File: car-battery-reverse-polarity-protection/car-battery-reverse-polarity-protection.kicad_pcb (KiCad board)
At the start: 2 copper layers, 64 x 75 mm, 10 parts, among them J1 Battery Connector, J2 Output, K1 AZ2150-1AE-24DEF

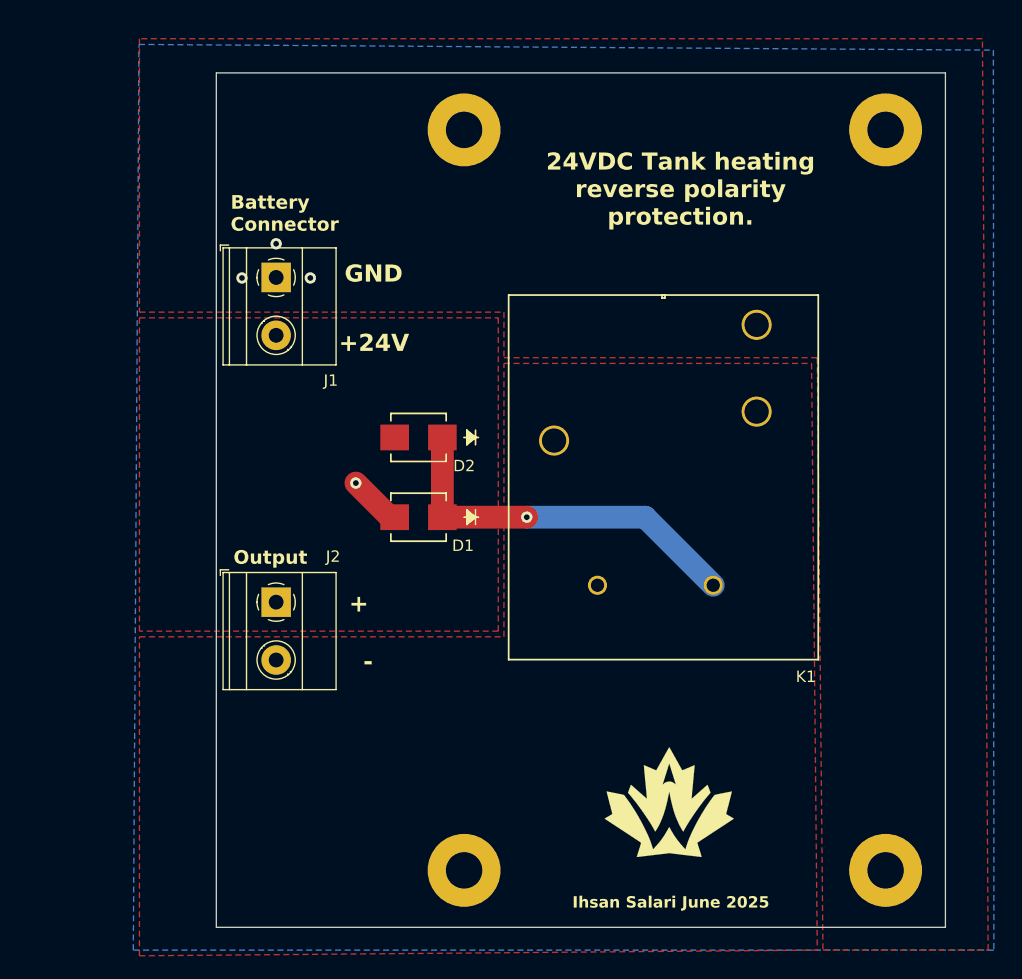
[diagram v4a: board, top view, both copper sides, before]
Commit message: Updated PCB size/mounting hole locations. Moved components around a little.
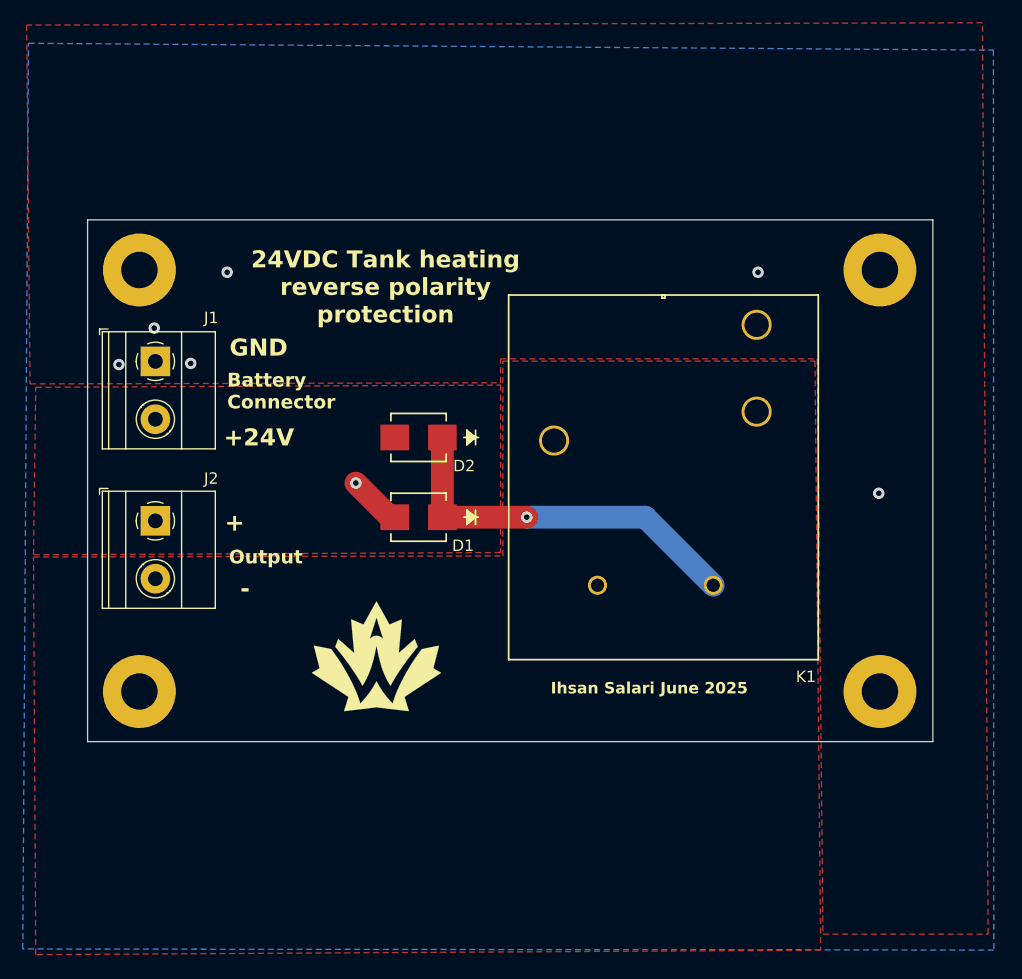
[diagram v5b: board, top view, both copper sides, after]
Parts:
- moved H5 32.5 mm to (104.0, 106.3)
- moved H3 31.0 mm to (104.0, 69.3)
- moved H4 28.7 mm to (124.8, 103.2)
- moved H2 15.7 mm to (169.0, 106.3)
- moved J1 12.9 mm to (105.4, 77.3)
- moved J2 12.8 mm to (105.4, 91.3)
- moved H1 12.3 mm to (169.0, 69.3)
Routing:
- net GND: vias 4 -> 7
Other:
- board size 64 x 75 mm -> 74.2 x 45.8 mm
- board text added: "24VDC Tank heating reverse polarity protection"
- board text removed: "24VDC Tank heating reverse polarity protection."
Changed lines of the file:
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@@
 			(outputformat 1)
 			(mirror no)
-			(drillshape 1)
+			(drillshape 0)
 			(scaleselection 1)
-			(outputdirectory "")
+			(outputdirectory "manufacture/")
 		)
 	)
@@
 	(footprint "ProjectLibrary:rocketry_logo_small_noletters"
 		(layer "F.Cu")
-		(at 150.5 116)
+		(at 124.8 103.2)
 		(property "Reference" "H4"
 			(at 0 0 0)
@@
 	(footprint "MountingHole:MountingHole_3.2mm_M3_Pad"
 		(layer "F.Cu")
-		(at 132.5 122)
+		(at 104 106.3)
 		(descr "Mounting Hole 3.2mm, M3")
 		(tags "mounting hole 3.2mm m3")
@@
 	(footprint "MountingHole:MountingHole_3.2mm_M3_Pad"
 		(layer "F.Cu")
-		(at 169.5 57)
+		(at 169 69.3)
 		(descr "Mounting Hole 3.2mm, M3")
 		(tags "mounting hole 3.2mm m3")
@@
 	(footprint "TerminalBlock_Phoenix:TerminalBlock_Phoenix_MKDS-1,5-2-5.08_1x02_P5.08mm_Horizontal"
 		(layer "F.Cu")
-		(at 116 69.955 -90)
+		(at 105.4 77.32 -90)
 		(descr "Terminal Block Phoenix MKDS-1,5-2-5.08, 2 pins, pitch 5.08mm, size 10.2x9.8mm^2, drill diamater 1.3mm, pad diameter 2.6mm, see http://www.farnell.com/datasheets/100425.pdf, script-generated using https://github.com/pointhi/kicad-footprint-generator/scripts/TerminalBlock_Phoenix")
 		(tags "THT Terminal Block Phoenix MKDS-1,5-2-5.08 pitch 5.08mm size 10.2x9.8mm^2 drill 1.3mm pad 2.6mm")
 		(property "Reference" "J1"
-			(at 9.045 -4.805 180)
+			(at -3.82 -4.9 180)
 			(layer "F.SilkS")
 			(effects
@@
 	(footprint "MountingHole:MountingHole_3.2mm_M3_Pad"
 		(layer "F.Cu")
-		(at 169.5 122)
+		(at 169 106.3)
 		(descr "Mounting Hole 3.2mm, M3")
 		(tags "mounting hole 3.2mm m3")
@@
 	(footprint "TerminalBlock_Phoenix:TerminalBlock_Phoenix_MKDS-1,5-2-5.08_1x02_P5.08mm_Horizontal"
 		(layer "F.Cu")
-		(at 116 98.455 -90)
+		(at 105.4 91.32 -90)
 		(descr "Terminal Block Phoenix MKDS-1,5-2-5.08, 2 pins, pitch 5.08mm, size 10.2x9.8mm^2, drill diamater 1.3mm, pad diameter 2.6mm, see http://www.farnell.com/datasheets/100425.pdf, script-generated using https://github.com/pointhi/kicad-footprint-generator/scripts/TerminalBlock_Phoenix")
 		(tags "THT Terminal Block Phoenix MKDS-1,5-2-5.08 pitch 5.08mm size 10.2x9.8mm^2 drill 1.3mm pad 2.6mm")
 		(property "Reference" "J2"
-			(at -4 -5 180)
+			(at -3.72 -4.9 180)
 			(layer "F.SilkS")
 			(effects
@@
 		)
 		(property "Value" "Output"
-			(at -3.92 0.5 180)
+			(at 3.18 -9.7 180)
 			(layer "F.SilkS")
 			(effects
@@
 	(footprint "MountingHole:MountingHole_3.2mm_M3_Pad"
 		(layer "B.Cu")
-		(at 132.5 57 180)
+		(at 104 69.3 180)
 		(descr "Mounting Hole 3.2mm, M3")
 		(tags "mounting hole 3.2mm m3")
@@
 	)
 	(gr_rect
-		(start 110.75 52)
-		(end 174.75 127)
+		(start 99.45 64.9)
+		(end 173.65 110.7)
 		(stroke
 			(width 0.05)
@@
 	)
 	(gr_text "+24V\n\n"
-		(at 121.5 79 0)
+		(at 111.4 87.3 0)
 		(layer "F.SilkS")
 		(effects
@@
 	)
 	(gr_text "+\n\n"
-		(at 126.5 99.5 90)
+		(at 115.6 92.4 90)
 		(layer "F.SilkS")
 		(effects
@@
 	)
 	(gr_text "Battery\nConnector"
-		(at 112 66 0)
+		(at 111.7 81.6 0)
 		(layer "F.SilkS")
 		(effects
@@
 	)
 	(gr_text "GND\n"
-		(at 122 70.5 0)
+		(at 111.9 77 0)
 		(layer "F.SilkS")
 		(effects
@@
 	)
 	(gr_text "Ihsan Salari June 2025\n\n"
-		(at 142 127 0)
+		(at 140.1 108.2 0)
 		(layer "F.SilkS")
 		(effects
@@
 	)
 	(gr_text "-"
-		(at 124.5 103 180)
+		(at 113.7 96.6 180)
 		(layer "F.SilkS")
 		(effects
@@
 		)
 	)
-	(gr_text "24VDC Tank heating\nreverse polarity\nprotection.\n"
-		(at 151.5 65.5 0)
+	(gr_text "24VDC Tank heating\nreverse polarity\nprotection\n\n"
+		(at 125.6 76.5 0)
 		(layer "F.SilkS")
 		(effects
@@
 	)
 	(via
-		(at 113 70)
+		(at 102.2 77.6)
+		(size 1)
+		(drill 0.5)
+		(layers "F.Cu" "B.Cu")
+		(free yes)
+		(net 1)
+	)
+	(via
+		(at 111.7 69.5)
 		(size 1)
 		(drill 0.5)
@@
 	)
 	(via
-		(at 119 70)
+		(at 158.3 69.5)
+		(size 1)
+		(drill 0.5)
+		(layers "F.Cu" "B.Cu")
+		(free yes)
+		(net 1)
+	)
+	(via
+		(at 168.9 88.9)
+		(size 1)
+		(drill 0.5)
+		(layers "F.Cu" "B.Cu")
+		(free yes)
+		(net 1)
+	)
+	(via
+		(at 108.5 77.5)
 		(size 1)
 		(drill 0.5)
@@
 	)
 	(via
-		(at 116 67)
+		(at 105.3 74.4)
 		(size 1)
 		(drill 0.5)
@@
 		(polygon
 			(pts
-				(xy 104 49) (xy 104 73) (xy 136 73) (xy 136 77) (xy 163.5 77) (xy 164 129) (xy 178.5 129) (xy 178 49)
+				(xy 94.1 47.8) (xy 94.4 79.3) (xy 135.7 79.2) (xy 135.7 77.1) (xy 163.5 77.1) (xy 164 127.6) (xy 178.5 127.6)
+				(xy 178 47.6)
 			)
 		)
@@
 		(polygon
 			(pts
-				(xy 104 101.5) (xy 136 101.5) (xy 136 77.5) (xy 163 77.5) (xy 163.5 129) (xy 104 129.5)
+				(xy 94.7 94.5) (xy 135.9 94.4) (xy 135.9 77.3) (xy 163.3 77.3) (xy 163.8 129) (xy 94.9 129.4)
 			)
 		)
@@
 		(polygon
 			(pts
-				(xy 104 73.5) (xy 135.5 73.5) (xy 135.5 101) (xy 104 101)
+				(xy 94.9 79.6) (xy 135.7 79.4) (xy 135.7 94.1) (xy 94.7 94.3)
 			)
 		)
@@
 		(polygon
 			(pts
-				(xy 103.961116 49.5) (xy 178.961116 50) (xy 179 129) (xy 103.461116 129)
+				(xy 94.261116 49.4) (xy 178.961116 50) (xy 179 129) (xy 93.761116 128.9)
 			)
 		)
